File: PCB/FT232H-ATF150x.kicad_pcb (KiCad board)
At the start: 2 copper layers, 42.5 x 27.9 mm, 21 parts, among them J1 CJMCU-232H, J2 JTAG-Altera, U1 ATF150x-xJx44, U2 MAX662A

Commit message: comments & silkscreen
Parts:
- J2: value JTAG-Altera -> Altera JTAG-A+VPP
- U1: value ATF150x-xJx44 -> ATF150x-xJx44 (PLCC-44)
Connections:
- net /OE1 renamed VPP
- R1 pad 1: +12V -> Net-(JP2-C)
- R1 pad 2: Net-(JP2-C) -> +12V
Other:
- board text added: "VPP"
- board text removed: "VPP/~{OE1}"

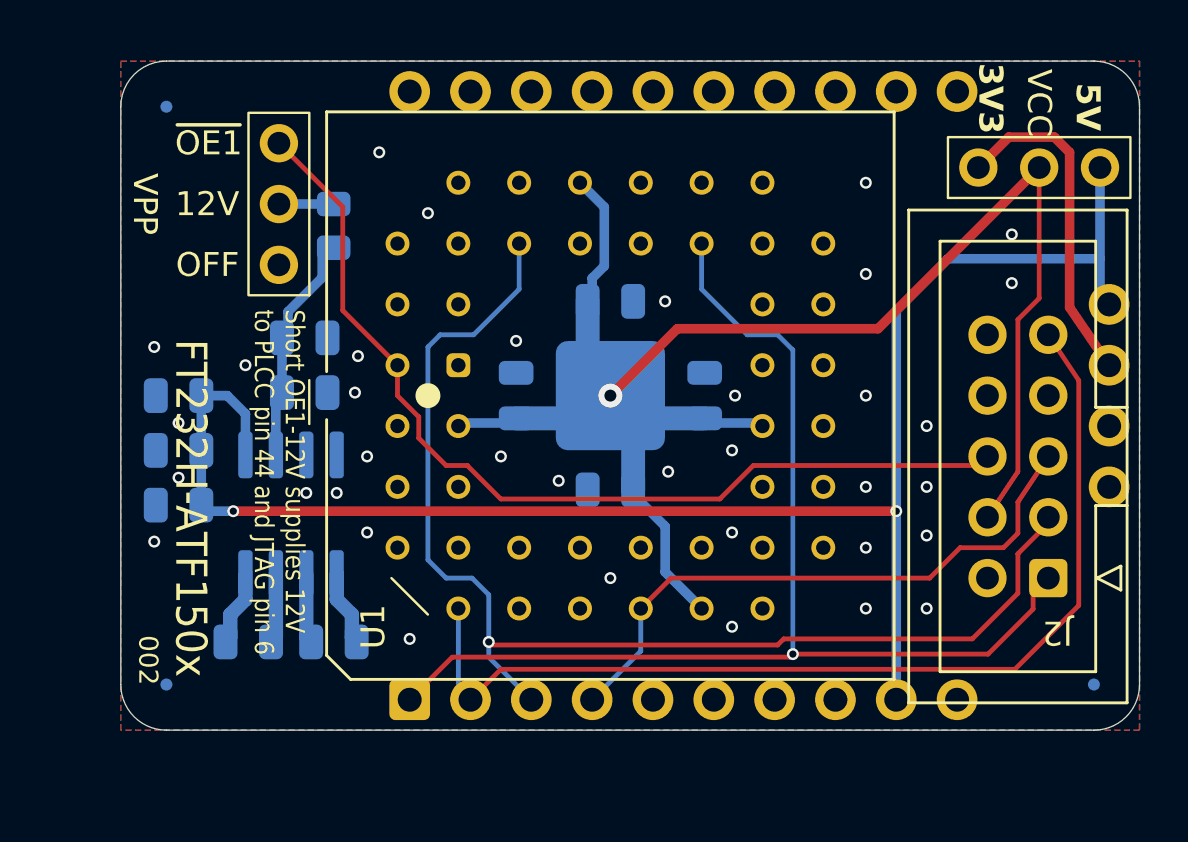
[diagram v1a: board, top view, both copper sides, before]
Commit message: reposition everything so jtag doesn't cover the FT232H module pins
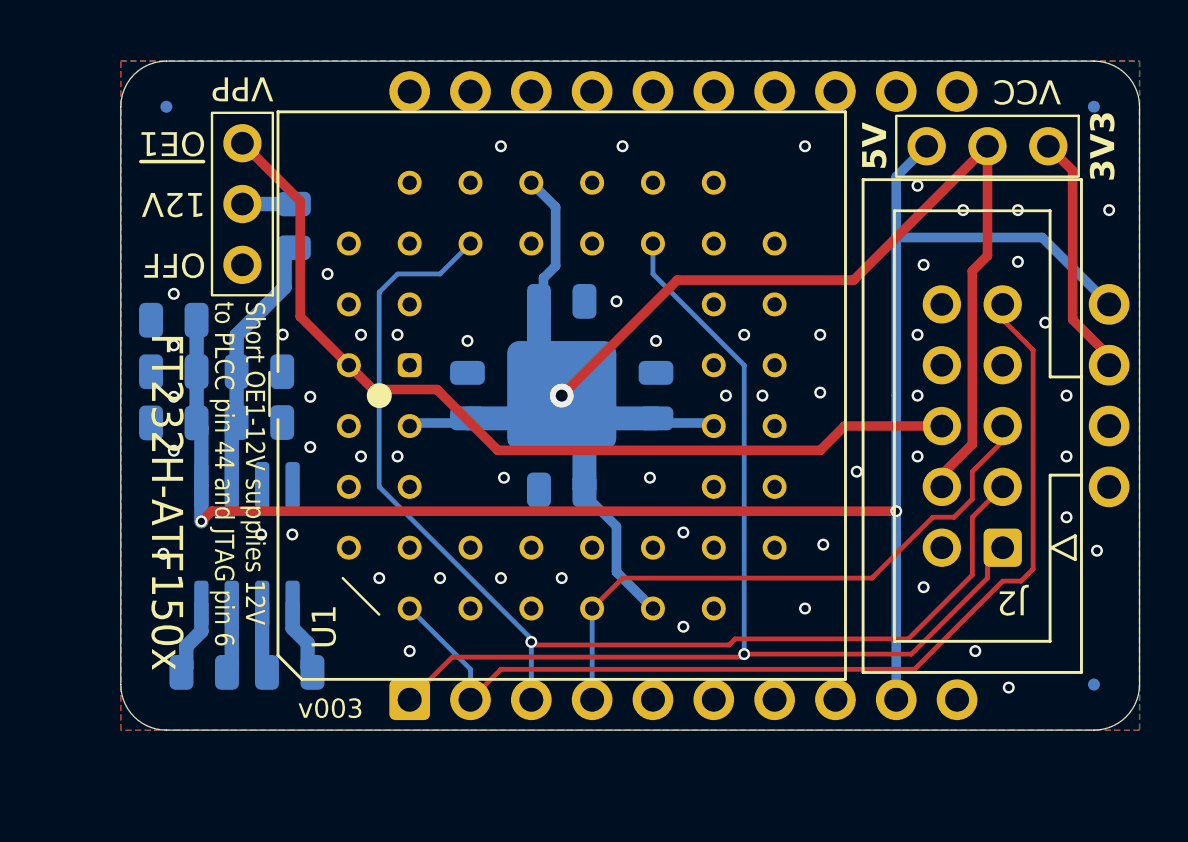
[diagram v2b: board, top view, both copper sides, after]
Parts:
- moved REF** 45.6 mm to (168.3, 89.5)
- moved C7 3.44 mm to (129.9, 102.7)
- moved C8 3.29 mm to (129.9, 100.6)
- moved C9 3.16 mm to (129.9, 98.5)
- moved JP1 3.05 mm to (166.4, 91.2), turned to -90 degrees
- moved C11 2.36 mm to (133.4, 100.6)
- moved J2 2.29 mm to (164.5, 108.0)
- moved C10 2.27 mm to (133.4, 102.7)
- moved C5 2.24 mm to (134.7, 113.2)
- moved U2 2.24 mm to (132.9, 107.8)
- moved C6 2.23 mm to (131.1, 113.2)
- moved C1 2.03 mm to (150.0, 101.6)
- moved C3 2.03 mm to (142.1, 101.6)
- moved U1 2.03 mm to (139.7, 100.3)
- moved C2 2.03 mm to (146.1, 105.5)
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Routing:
- net +3V3: track 14.0 -> 10.2 mm
- net VPP: track 40.3 -> 37.8 mm
- net TDO: track 50.6 -> 48.2 mm
- net +5V: track 69.1 -> 71.4 mm
- net TCK: track 48.6 -> 46.5 mm
- net +12V: track 9.94 -> 11.2 mm
- net TDI: track 42.7 -> 42.2 mm
- net GND: vias 36 -> 55
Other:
- board text added: "v${REVISION}"
- board text removed: "${REVISION}"
